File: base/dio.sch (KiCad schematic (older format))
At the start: 0 parts

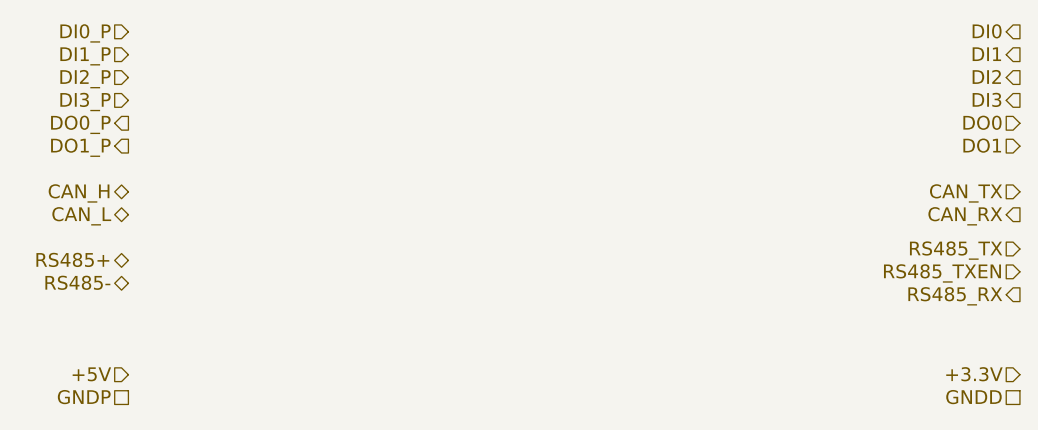
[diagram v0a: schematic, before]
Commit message: 1. Separate dio_can_rs485 sheet into two: dio + can_rs485. 2. Move can and rs485 into digital power domain 3. Add CAN transiever to can_rs485 sheet
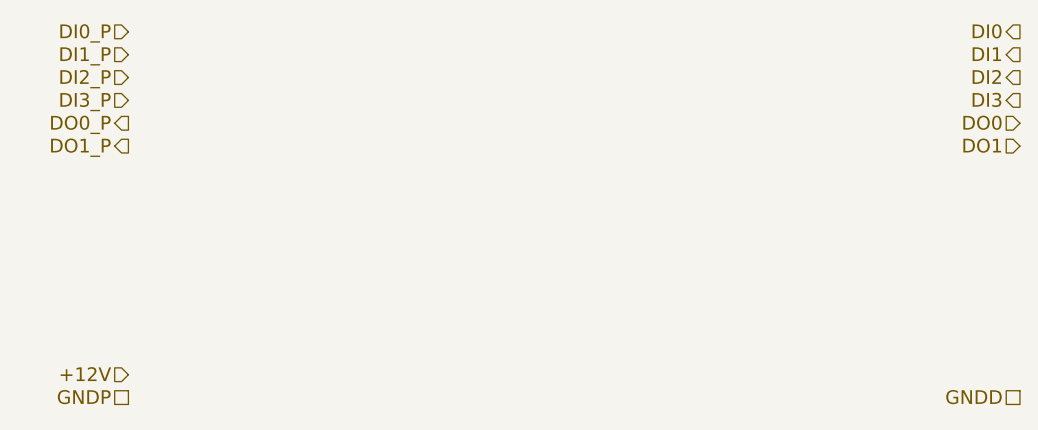
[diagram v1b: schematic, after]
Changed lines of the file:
@@
 LIBS:dc-dc
 LIBS:regul
+LIBS:interface
+LIBS:ESD_Protection
 LIBS:4hbd-base-cache
 EELAYER 25 0
@@
 $Descr A4 11693 8268
 encoding utf-8
-Sheet 3 8
+Sheet 3 9
 Title ""
 Date ""
@@
 Text HLabel 3000 2800 0    60   Output ~ 0
 DO1_P
-Text HLabel 3000 3000 0    60   BiDi ~ 0
-CAN_H
-Text HLabel 3000 3100 0    60   BiDi ~ 0
-CAN_L
-Text HLabel 3000 3300 0    60   BiDi ~ 0
-RS485+
-Text HLabel 3000 3400 0    60   BiDi ~ 0
-RS485-
 Text HLabel 6900 2300 0    60   Output ~ 0
 DI0
@@
 Text HLabel 6900 2800 0    60   Input ~ 0
 DO1
-Text HLabel 6900 3000 0    60   Input ~ 0
-CAN_TX
-Text HLabel 6900 3100 0    60   Output ~ 0
-CAN_RX
-Text HLabel 6900 3250 0    60   Input ~ 0
-RS485_TX
-Text HLabel 6900 3350 0    60   Input ~ 0
-RS485_TXEN
-Text HLabel 6900 3450 0    60   Output ~ 0
-RS485_RX
-Text HLabel 6900 3800 0    60   Input ~ 0
-+3.3V
 Text HLabel 6900 3900 0    60   UnSpc ~ 0
 GNDD
 Text HLabel 3000 3800 0    60   Input ~ 0
-+5V
++12V
 Text HLabel 3000 3900 0    60   UnSpc ~ 0
 GNDP

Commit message: dio.sch was updated
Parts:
- added D? (x6): LED, symbol LED
- added D? (x2): BZT52C30, symbol D
- added F? (x2): Fuse 200mA, symbol Fuse
- added Q? (x2): 2N7002, symbol Q_NMOS_GSD
- added R? (x6): 2k2, symbol R
- added R? (x2): 330, symbol R
- added R? (x2): 3k3, symbol R
- added U? (x6): MOCD217M, Housings_SOIC:SOIC-8_3.9x4.9mm_Pitch1.27mm, symbol MOCD217M
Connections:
- wire segments 0 -> 86

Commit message: fix
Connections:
- wire segments 86 -> 65
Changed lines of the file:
@@
 	3650 6300 3850 6300
 Wire Wire Line
-	2650 6500 3750 6500
+	2650 6500 3850 6500
 Wire Wire Line
-	3750 6500 3850 6500
-Wire Wire Line
-	3750 5100 3750 5550
-Wire Wire Line
-	3750 5550 3750 6050
-Wire Wire Line
-	3750 6050 3750 6500
+	3750 5100 3750 6500
 Wire Wire Line
 	3750 6050 3850 6050
@@
 	4850 6300 4450 6300
 Wire Wire Line
-	4450 6500 4600 6500
+	4450 6500 5150 6500
 Wire Wire Line
-	4600 6500 5150 6500
-Wire Wire Line
-	4600 5100 4600 5550
-Wire Wire Line
-	4600 5550 4600 6050
-Wire Wire Line
-	4600 6050 4600 6500
+	4600 5100 4600 6500
 Wire Wire Line
 	4600 6050 4450 6050
@@
 	1050 1050 1750 1050
 Wire Wire Line
-	3950 2000 4350 2000
-Wire Wire Line
-	4350 2000 4850 2000
-Wire Wire Line
-	4850 2000 4950 2000
+	3950 2000 4950 2000
 Wire Wire Line
 	4350 2050 4350 2000
@@
 	4350 2500 4450 2500
 Wire Wire Line
-	4750 2500 4850 2500
-Wire Wire Line
-	4850 2500 5250 2500
-Wire Wire Line
-	5250 2500 5800 2500
-Wire Wire Line
-	5800 2500 6550 2500
+	4750 2500 6550 2500
 Wire Wire Line
 	5250 2200 5250 2500
@@
 	5250 1800 5250 1650
 Wire Wire Line
-	5250 1650 5800 1650
-Wire Wire Line
-	5800 1650 5900 1650
+	5250 1650 5900 1650
 Wire Wire Line
 	5800 1850 5800 1650
@@
 	6200 1650 6550 1650
 Wire Wire Line
-	3950 3350 4350 3350
-Wire Wire Line
-	4350 3350 4850 3350
-Wire Wire Line
-	4850 3350 4950 3350
+	3950 3350 4950 3350
 Wire Wire Line
 	4350 3400 4350 3350
@@
 	4350 3850 4450 3850
 Wire Wire Line
-	4750 3850 4850 3850
-Wire Wire Line
-	4850 3850 5250 3850
-Wire Wire Line
-	5250 3850 5800 3850
-Wire Wire Line
-	5800 3850 6550 3850
+	4750 3850 6550 3850
 Wire Wire Line
 	5250 3550 5250 3850
@@
 	5250 3150 5250 3000
 Wire Wire Line
-	5250 3000 5800 3000
-Wire Wire Line
-	5800 3000 5900 3000
+	5250 3000 5900 3000
 Wire Wire Line
 	5800 3200 5800 3000
@@
 	6550 1400 4150 1400
 Wire Wire Line
-	4150 1400 4150 1800
-Wire Wire Line
-	4150 1800 4150 3150
+	4150 1400 4150 3150
 Wire Wire Line
 	4150 1800 3950 1800
@@
 	3250 2000 3250 3350
 Wire Wire Line
-	3250 3350 3250 3350
-Wire Wire Line
-	3250 3350 2300 3350
-Wire Wire Line
-	3350 3350 3250 3350
+	2300 3350 3350 3350
 Connection ~ 3250 3350
 Text Label 2300 3350 0    60   ~ 0
